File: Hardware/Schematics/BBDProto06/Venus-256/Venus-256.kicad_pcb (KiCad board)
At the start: 2 copper layers, 172.7 x 109.2 mm, 227 parts, among them J201 RaspberryPi header, J301 ARM JTAG, U1001 AD7616, U101 TPS22993, U401 AD7616, U501 ATSAME70Q21A-AN, U601 AD7616, U701 AD7616, U801 AD7616, U901 ATSAME70Q21A-AN

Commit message: Switched from 2 layer to 4 layer design
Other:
- copper layers 2 -> 4

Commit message: Added the SensorLine net class
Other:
- net class SensorLine added: clearance 0.4, trace_width 0.4, via_dia 0.6, via_drill 0.4
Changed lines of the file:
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@@
     (add_net "Net-(JP101-Pad1)")
     (add_net "Net-(JP102-Pad1)")
+  )
+  (net_class SensorLine ""
+    (clearance 0.4)
+    (trace_width 0.4)
+    (via_dia 0.6)
+    (via_drill 0.4)
+    (uvia_dia 0.3)
+    (uvia_drill 0.1)
     (add_net "Net-(TP1002-Pad1)")
     (add_net "Net-(TP1003-Pad1)")

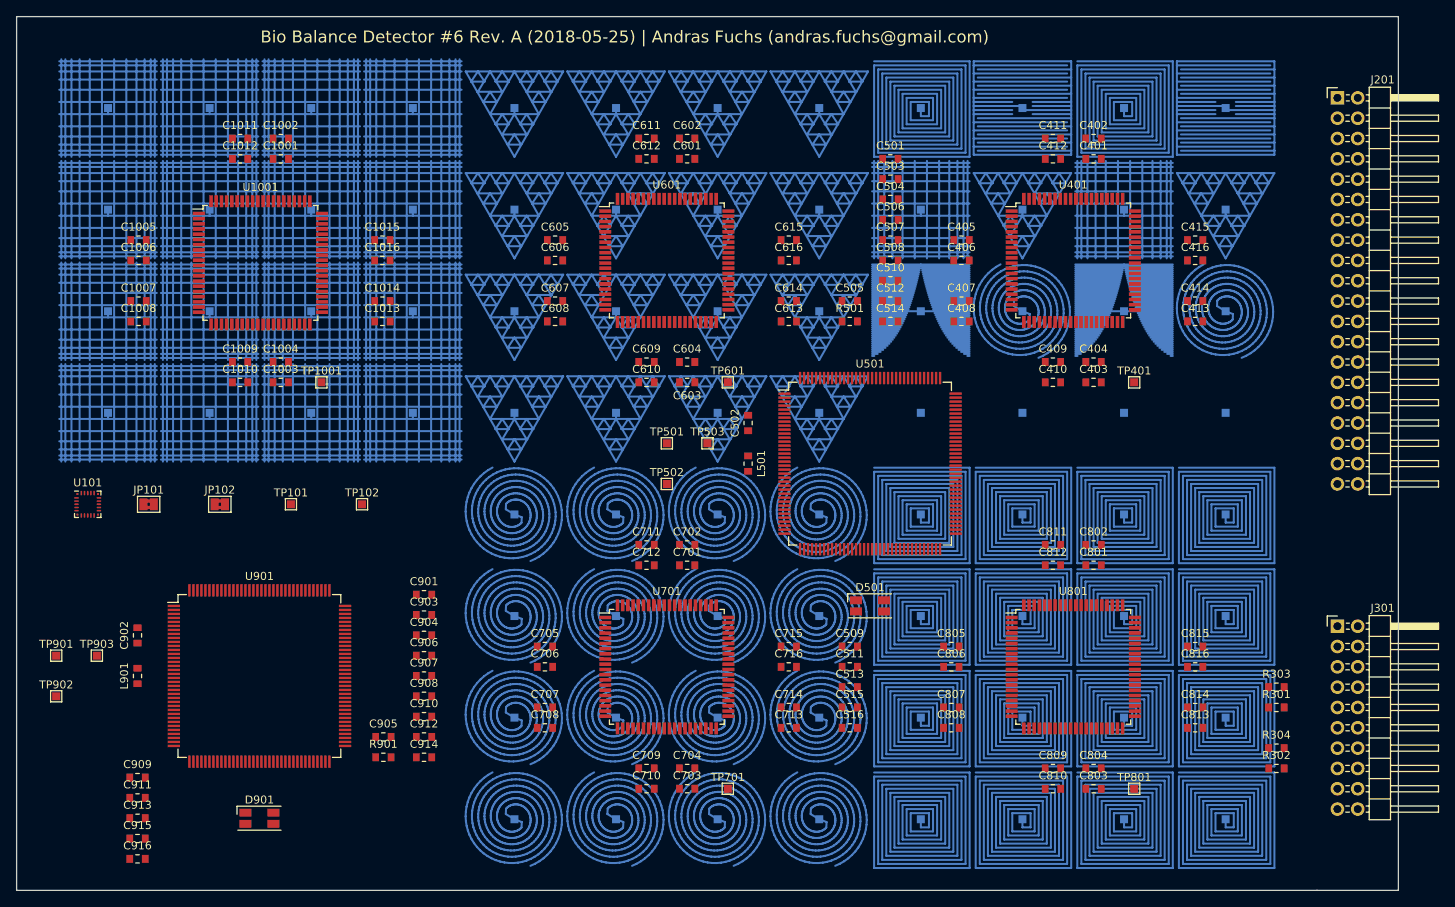
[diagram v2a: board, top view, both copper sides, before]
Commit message: Added the jumper for the ground pads
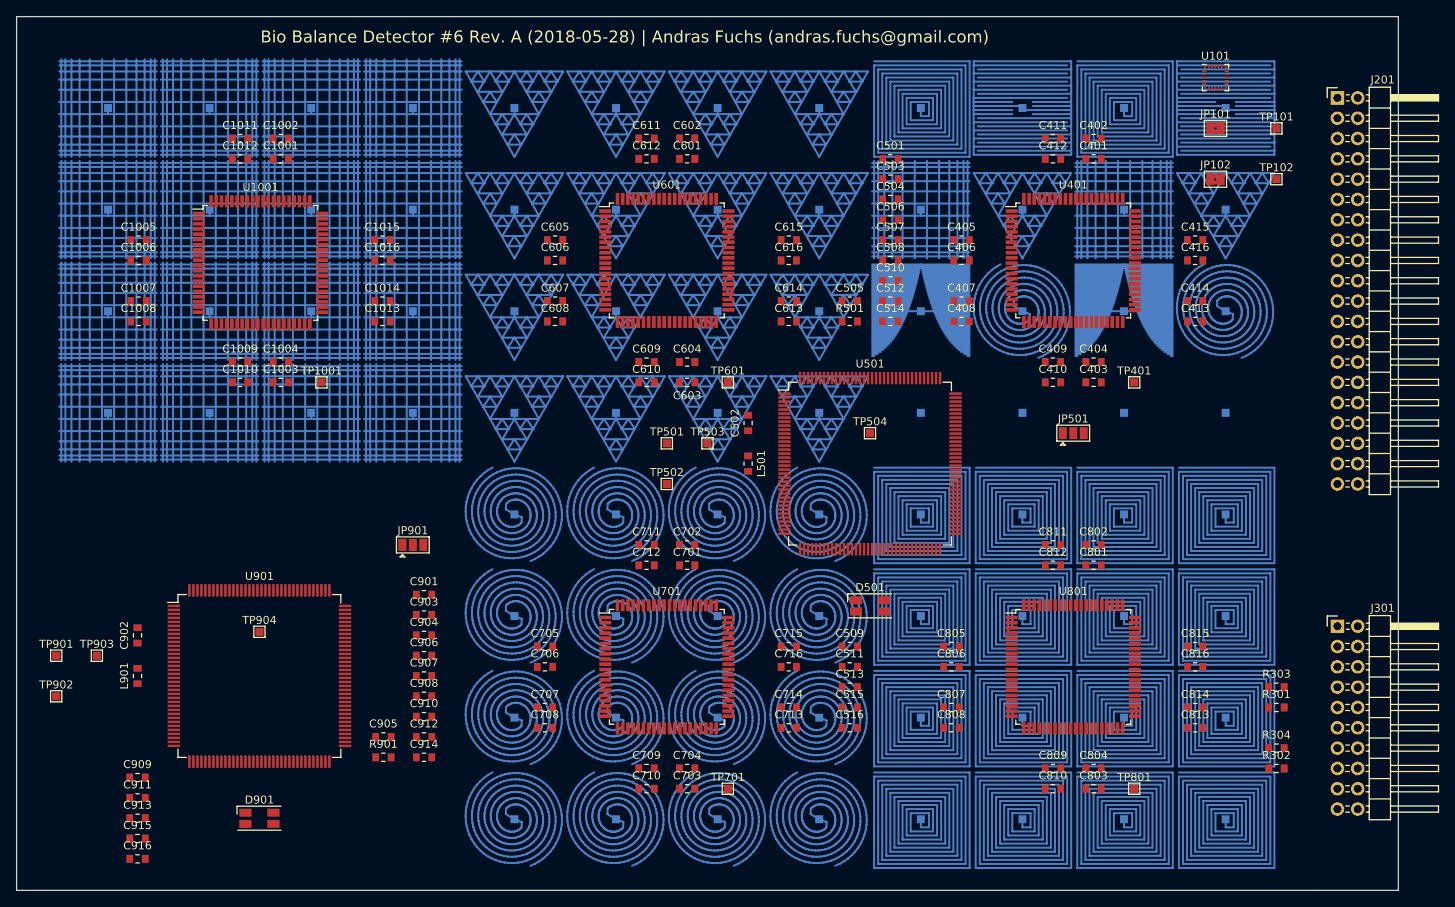
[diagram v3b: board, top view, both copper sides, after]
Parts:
- added JP501: GPAD_JP, Jumper:SolderJumper-3_P1.3mm_Open_Pad1.0x1.5mm, F.Cu at (147.3, 67.3)
- added JP901: GPAD_JP, Jumper:SolderJumper-3_P1.3mm_Open_Pad1.0x1.5mm, F.Cu at (64.8, 81.3)
- added TP504: GPAD, TestPoint:TestPoint_Pad_1.0x1.0mm, F.Cu at (121.9, 67.3)
- added TP904: GPAD, TestPoint:TestPoint_Pad_1.0x1.0mm, F.Cu at (45.6, 92.1)
- moved U101 150.7 mm to (165.1, 22.9)
- moved JP101 141.4 mm to (165.1, 29.2)
- moved TP101 131.8 mm to (172.7, 29.2)
- moved JP102 130.9 mm to (165.1, 35.6)
- moved TP102 121.3 mm to (172.7, 35.6)
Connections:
- U501 pad 1: (no net) -> Net-(JP501-Pad1)
- U901 pad 1: (no net) -> Net-(JP901-Pad1)
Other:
- board text added: "Bio Balance Detector #6 Rev. A (2018-05-28) | Andras Fuchs (andras.fuchs@gmail.com)"
- board text removed: "Bio Balance Detector #6 Rev. A (2018-05-25) | Andras Fuchs (andras.fuchs@gmail.com)"
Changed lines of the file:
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@@
     (tracks 9412)
     (zones 0)
-    (modules 227)
-    (nets 163)
+    (modules 231)
+    (nets 167)
   )
   (page A4)
@@
     (1 In1.Cu signal)
     (2 In2.Cu signal)
-    (31 B.Cu signal)
+    (31 B.Cu signal hide)
     (33 F.Adhes user)
     (35 F.Paste user)
-    (36 B.SilkS user)
+    (36 B.SilkS user hide)
     (37 F.SilkS user)
     (39 F.Mask user)
@@
     (44 Edge.Cuts user)
     (45 Margin user)
-    (46 B.CrtYd user)
+    (46 B.CrtYd user hide)
     (47 F.CrtYd user)
     (49 F.Fab user)
@@
     (via_min_size 0.4)
     (via_min_drill 0.3)
+    (blind_buried_vias_allowed yes)
     (uvia_size 0.3)
     (uvia_drill 0.1)
@@
   (net 161 "Net-(JP102-Pad1)")
   (net 162 "Net-(JP101-Pad1)")
+  (net 163 "Net-(JP501-Pad1)")
+  (net 164 "Net-(JP501-Pad2)")
+  (net 165 "Net-(JP901-Pad2)")
+  (net 166 "Net-(JP901-Pad1)")
   (net_class Default "This is the default net class."
     (clearance 0.254)
@@
     (add_net "Net-(JP101-Pad1)")
     (add_net "Net-(JP102-Pad1)")
+    (add_net "Net-(JP501-Pad1)")
+    (add_net "Net-(JP501-Pad2)")
+    (add_net "Net-(JP901-Pad1)")
+    (add_net "Net-(JP901-Pad2)")
   )
   (net_class SensorLine ""
@@
     (pad 3 smd rect (at -10.7 -7.75) (size 1.55 0.3) (layers F.Cu F.Paste F.Mask))
     (pad 2 smd rect (at -10.7 -8.25) (size 1.55 0.3) (layers F.Cu F.Paste F.Mask))
-    (pad 1 smd rect (at -10.7 -8.75) (size 1.55 0.3) (layers F.Cu F.Paste F.Mask))
+    (pad 1 smd rect (at -10.7 -8.75) (size 1.55 0.3) (layers F.Cu F.Paste F.Mask)
+      (net 163 "Net-(JP501-Pad1)"))
     (model ${KISYS3DMOD}/Package_QFP.3dshapes/LQFP-144_20x20mm_P0.5mm.wrl
       (at (xyz 0 0 0))
@@
     (fp_line (start 10.175 -10.175) (end 9.125 -10.175) (layer F.SilkS) (width 0.15))
     (fp_line (start -10.175 -9.2) (end -11.475 -9.2) (layer F.SilkS) (width 0.15))
-    (pad 1 smd rect (at -10.7 -8.75) (size 1.55 0.3) (layers F.Cu F.Paste F.Mask))
+    (pad 1 smd rect (at -10.7 -8.75) (size 1.55 0.3) (layers F.Cu F.Paste F.Mask)
+      (net 166 "Net-(JP901-Pad1)"))
     (pad 2 smd rect (at -10.7 -8.25) (size 1.55 0.3) (layers F.Cu F.Paste F.Mask))
     (pad 3 smd rect (at -10.7 -7.75) (size 1.55 0.3) (layers F.Cu F.Paste F.Mask))
@@
   )
   (module TestPoint:TestPoint_Pad_1.0x1.0mm (layer F.Cu)
-    (at 49.53 76.2)
+    (at 172.72 29.21)
     (descr "SMD rectangular pad as test Point, square 1.0mm side length")
     (tags "test point SMD pad rectangle square")
@@
   )
   (module TestPoint:TestPoint_Pad_1.0x1.0mm (layer F.Cu)
-    (at 58.42 76.2)
+    (at 172.72 35.56)
     (descr "SMD rectangular pad as test Point, square 1.0mm side length")
     (tags "test point SMD pad rectangle square")
@@
   )
   (module Package_DFN_QFN:Texas_S-PWQFN-N20 (layer F.Cu)
-    (at 24.13 76.2)
+    (at 165.1 22.86)
     (descr "20-Pin Plastic Quad Flatpack No-Lead Package, Body 3.0x3.0x0.8mm, Texas Instruments (http://www.ti.com/lit/ds/symlink/tps22993.pdf)")
     (tags "QFN 0.4")
@@
   )
   (module Jumper:SolderJumper-2_P1.3mm_Bridged2Bar_Pad1.0x1.5mm (layer F.Cu)
-    (at 31.75 76.2)
+    (at 165.1 29.21)
     (descr "SMD Solder Jumper, 1x1.5mm Pads, 0.3mm gap, bridged with 2 copper strips")
     (tags "solder jumper open")
@@
   )
   (module Jumper:SolderJumper-2_P1.3mm_Bridged2Bar_Pad1.0x1.5mm (layer F.Cu)
-    (at 40.64 76.2)
+    (at 165.1 35.56)
     (descr "SMD Solder Jumper, 1x1.5mm Pads, 0.3mm gap, bridged with 2 copper strips")
     (tags "solder jumper open")
@@
       (net 161 "Net-(JP102-Pad1)"))
   )
+  (module Jumper:SolderJumper-3_P1.3mm_Open_Pad1.0x1.5mm (layer F.Cu)
+    (at 147.32 67.31)
+    (descr "SMD Solder 3-pad Jumper, 1x1.5mm Pads, 0.3mm gap, open")
+    (tags "solder jumper open")
+    (attr virtual)
+    (fp_text reference JP501 (at 0 -1.8) (layer F.SilkS)
+      (effects (font (size 1 1) (thickness 0.15)))
+    )
+    (fp_text value GPAD_JP (at 0 2) (layer F.Fab)
+      (effects (font (size 1 1) (thickness 0.15)))
+    )
+    (fp_line (start 2.3 1.25) (end -2.3 1.25) (layer F.CrtYd) (width 0.05))
+    (fp_line (start 2.3 1.25) (end 2.3 -1.25) (layer F.CrtYd) (width 0.05))
+    (fp_line (start -2.3 -1.25) (end -2.3 1.25) (layer F.CrtYd) (width 0.05))
+    (fp_line (start -2.3 -1.25) (end 2.3 -1.25) (layer F.CrtYd) (width 0.05))
+    (fp_line (start -2.05 -1) (end 2.05 -1) (layer F.SilkS) (width 0.12))
+    (fp_line (start 2.05 -1) (end 2.05 1) (layer F.SilkS) (width 0.12))
+    (fp_line (start 2.05 1) (end -2.05 1) (layer F.SilkS) (width 0.12))
+    (fp_line (start -2.05 1) (end -2.05 -1) (layer F.SilkS) (width 0.12))
+    (fp_line (start -1.3 1.2) (end -1.6 1.5) (layer F.SilkS) (width 0.12))
+    (fp_line (start -1.6 1.5) (end -1 1.5) (layer F.SilkS) (width 0.12))
+    (fp_line (start -1.3 1.2) (end -1 1.5) (layer F.SilkS) (width 0.12))
+    (pad 1 smd rect (at -1.3 0) (size 1 1.5) (layers F.Cu F.Mask)
+      (net 163 "Net-(JP501-Pad1)"))
+    (pad 2 smd rect (at 0 0) (size 1 1.5) (layers F.Cu F.Mask)
+      (net 164 "Net-(JP501-Pad2)"))
+    (pad 3 smd rect (at 1.3 0) (size 1 1.5) (layers F.Cu F.Mask)
+      (net 1 GND))
+  )
+  (module Jumper:SolderJumper-3_P1.3mm_Open_Pad1.0x1.5mm (layer F.Cu)
+    (at 64.77 81.28)
+    (descr "SMD Solder 3-pad Jumper, 1x1.5mm Pads, 0.3mm gap, open")
+    (tags "solder jumper open")
+    (attr virtual)
+    (fp_text reference JP901 (at 0 -1.8) (layer F.SilkS)
+      (effects (font (size 1 1) (thickness 0.15)))
+    )
+    (fp_text value GPAD_JP (at 0 2) (layer F.Fab)
+      (effects (font (size 1 1) (thickness 0.15)))
+    )
+    (fp_line (start -1.3 1.2) (end -1 1.5) (layer F.SilkS) (width 0.12))
+    (fp_line (start -1.6 1.5) (end -1 1.5) (layer F.SilkS) (width 0.12))
+    (fp_line (start -1.3 1.2) (end -1.6 1.5) (layer F.SilkS) (width 0.12))
+    (fp_line (start -2.05 1) (end -2.05 -1) (layer F.SilkS) (width 0.12))
+    (fp_line (start 2.05 1) (end -2.05 1) (layer F.SilkS) (width 0.12))
+    (fp_line (start 2.05 -1) (end 2.05 1) (layer F.SilkS) (width 0.12))
+    (fp_line (start -2.05 -1) (end 2.05 -1) (layer F.SilkS) (width 0.12))
+    (fp_line (start -2.3 -1.25) (end 2.3 -1.25) (layer F.CrtYd) (width 0.05))
+    (fp_line (start -2.3 -1.25) (end -2.3 1.25) (layer F.CrtYd) (width 0.05))
+    (fp_line (start 2.3 1.25) (end 2.3 -1.25) (layer F.CrtYd) (width 0.05))
+    (fp_line (start 2.3 1.25) (end -2.3 1.25) (layer F.CrtYd) (width 0.05))
+    (pad 3 smd rect (at 1.3 0) (size 1 1.5) (layers F.Cu F.Mask)
+      (net 1 GND))
+    (pad 2 smd rect (at 0 0) (size 1 1.5) (layers F.Cu F.Mask)
+      (net 165 "Net-(JP901-Pad2)"))
+    (pad 1 smd rect (at -1.3 0) (size 1 1.5) (layers F.Cu F.Mask)
+      (net 166 "Net-(JP901-Pad1)"))
+  )
+  (module TestPoint:TestPoint_Pad_1.0x1.0mm (layer F.Cu)
+    (at 121.92 67.31)
+    (descr "SMD rectangular pad as test Point, square 1.0mm side length")
+    (tags "test point SMD pad rectangle square")
+    (attr virtual)
+    (fp_text reference TP504 (at 0 -1.448) (layer F.SilkS)
+      (effects (font (size 1 1) (thickness 0.15)))
+    )
+    (fp_text value GPAD (at 0 1.55) (layer F.Fab)
+      (effects (font (size 1 1) (thickness 0.15)))
+    )
+    (fp_line (start 1 1) (end -1 1) (layer F.CrtYd) (width 0.05))
+    (fp_line (start 1 1) (end 1 -1) (layer F.CrtYd) (width 0.05))
+    (fp_line (start -1 -1) (end -1 1) (layer F.CrtYd) (width 0.05))
+    (fp_line (start -1 -1) (end 1 -1) (layer F.CrtYd) (width 0.05))
+    (fp_line (start -0.7 0.7) (end -0.7 -0.7) (layer F.SilkS) (width 0.12))
+    (fp_line (start 0.7 0.7) (end -0.7 0.7) (layer F.SilkS) (width 0.12))
+    (fp_line (start 0.7 -0.7) (end 0.7 0.7) (layer F.SilkS) (width 0.12))
+    (fp_line (start -0.7 -0.7) (end 0.7 -0.7) (layer F.SilkS) (width 0.12))
+    (fp_text user %R (at 0 -1.45) (layer F.Fab)
+      (effects (font (size 1 1) (thickness 0.15)))
+    )
+    (pad 1 smd rect (at 0 0) (size 1 1) (layers F.Cu F.Mask)
+      (net 164 "Net-(JP501-Pad2)"))
+  )
+  (module TestPoint:TestPoint_Pad_1.0x1.0mm (layer F.Cu)
+    (at 45.595524 92.1405)
+    (descr "SMD rectangular pad as test Point, square 1.0mm side length")
+    (tags "test point SMD pad rectangle square")
+    (attr virtual)
+    (fp_text reference TP904 (at 0 -1.448) (layer F.SilkS)
+      (effects (font (size 1 1) (thickness 0.15)))
+    )
+    (fp_text value GPAD (at 0 1.55) (layer F.Fab)
+      (effects (font (size 1 1) (thickness 0.15)))
+    )
+    (fp_text user %R (at 0 -1.45) (layer F.Fab)
+      (effects (font (size 1 1) (thickness 0.15)))
+    )
+    (fp_line (start -0.7 -0.7) (end 0.7 -0.7) (layer F.SilkS) (width 0.12))
+    (fp_line (start 0.7 -0.7) (end 0.7 0.7) (layer F.SilkS) (width 0.12))
+    (fp_line (start 0.7 0.7) (end -0.7 0.7) (layer F.SilkS) (width 0.12))
+    (fp_line (start -0.7 0.7) (end -0.7 -0.7) (layer F.SilkS) (width 0.12))
+    (fp_line (start -1 -1) (end 1 -1) (layer F.CrtYd) (width 0.05))
+    (fp_line (start -1 -1) (end -1 1) (layer F.CrtYd) (width 0.05))
+    (fp_line (start 1 1) (end 1 -1) (layer F.CrtYd) (width 0.05))
+    (fp_line (start 1 1) (end -1 1) (layer F.CrtYd) (width 0.05))
+    (pad 1 smd rect (at 0 0) (size 1 1) (layers F.Cu F.Mask)
+      (net 165 "Net-(JP901-Pad2)"))
+  )
   (dimension 172.72 (width 0.3) (layer Dwgs.User)
     (gr_text "172.720 mm" (at 101.6 129.1) (layer Dwgs.User)
@@
   (gr_line (start 20.32 20.32) (end 33.02 20.32) (layer B.SilkS) (width 0.4))
   (gr_line (start 15.24 124.46) (end 15.24 15.24) (layer Edge.Cuts) (width 0.15))
-  (gr_text "Bio Balance Detector #6 Rev. A (2018-05-25) | Andras Fuchs (andras.fuchs@gmail.com)" (at 45.72 17.78) (layer F.SilkS)
+  (gr_text "Bio Balance Detector #6 Rev. A (2018-05-28) | Andras Fuchs (andras.fuchs@gmail.com)" (at 45.72 17.78) (layer F.SilkS)
     (effects (font (size 1.5 1.5) (thickness 0.3)) (justify left))
   )
